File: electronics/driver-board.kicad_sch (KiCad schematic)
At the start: 51 parts, among them J2 Conn_01x05_Socket, J3 S4B-XH-A, J4 Qwiic_RA, J5 Conn_01x06_Female, J6 Conn_01x05_Socket, J7 Conn_01x02, SW1 SW_Push, SW2 SW_Push, SW3 SW_Push, SW4 SW_Push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

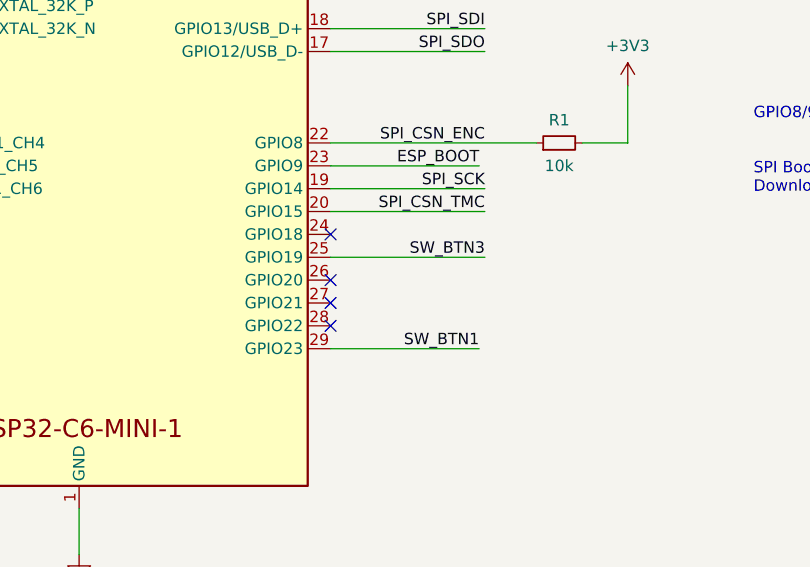
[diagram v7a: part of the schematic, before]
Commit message: moved few tracks and changed track width from 0.2 -> 0.25
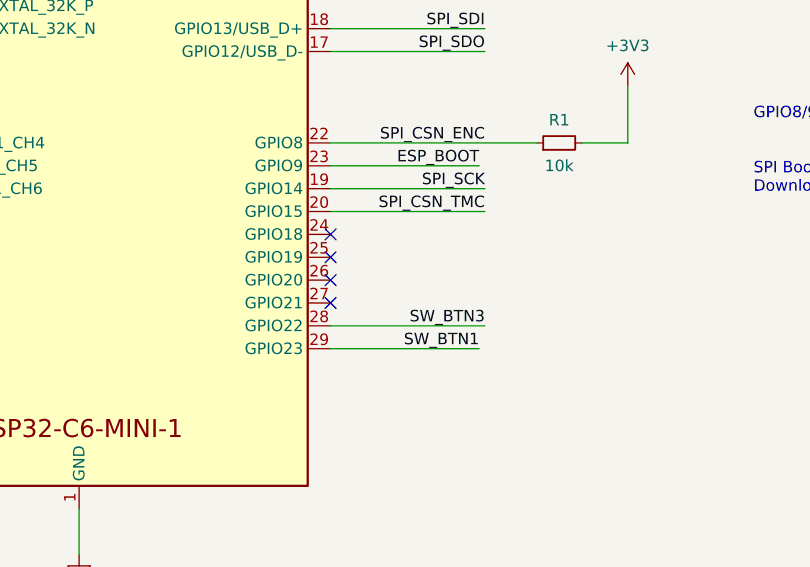
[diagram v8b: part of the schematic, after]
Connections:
- net SW_BTN3: now also U3.28 (GPIO22); no longer U3.25 (GPIO19)
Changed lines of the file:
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@@
   (no_connect (at 196.85 182.245))
   (no_connect (at 312.42 99.695))
+  (no_connect (at 312.42 94.615))
   (no_connect (at 194.945 71.755))
   (no_connect (at 117.475 184.785))
   (no_connect (at 256.54 74.295))
   (no_connect (at 117.475 182.245))
-  (no_connect (at 312.42 102.235))
   (no_connect (at 61.595 174.625))
   (no_connect (at 196.85 187.325))
@@
     (stroke (width 0) (type default))
   )
-  (wire (pts (xy 312.42 94.615) (xy 329.565 94.615))
+  (wire (pts (xy 312.42 102.235) (xy 329.565 102.235))
     (stroke (width 0) (type default))
   )
@@
     (effects (font (size 1.27 1.27)) (justify left bottom))
   )
-  (label "SW_BTN3" (at 329.565 94.615 180) (fields_autoplaced)
-    (effects (font (size 1.27 1.27)) (justify right bottom))
-  )
+  (label "SW_BTN3" (at 329.565 102.235 180) (fields_autoplaced)
+    (effects (font (size 1.27 1.27)) (justify right bottom))
+  )
